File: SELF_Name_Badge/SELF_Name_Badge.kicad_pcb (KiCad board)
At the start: 2 copper layers, 105 x 70 mm, 1 part

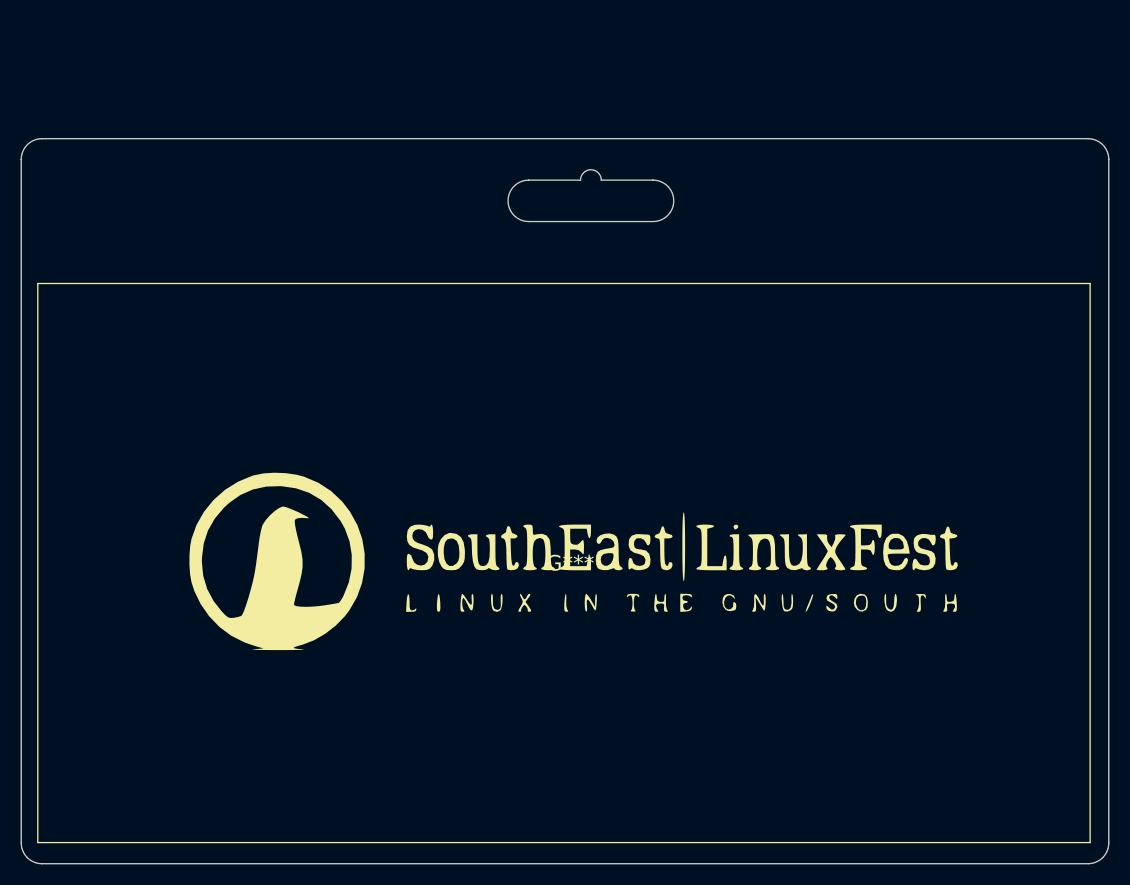
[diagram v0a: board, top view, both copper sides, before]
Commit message: cutout for adafruit QT esp32
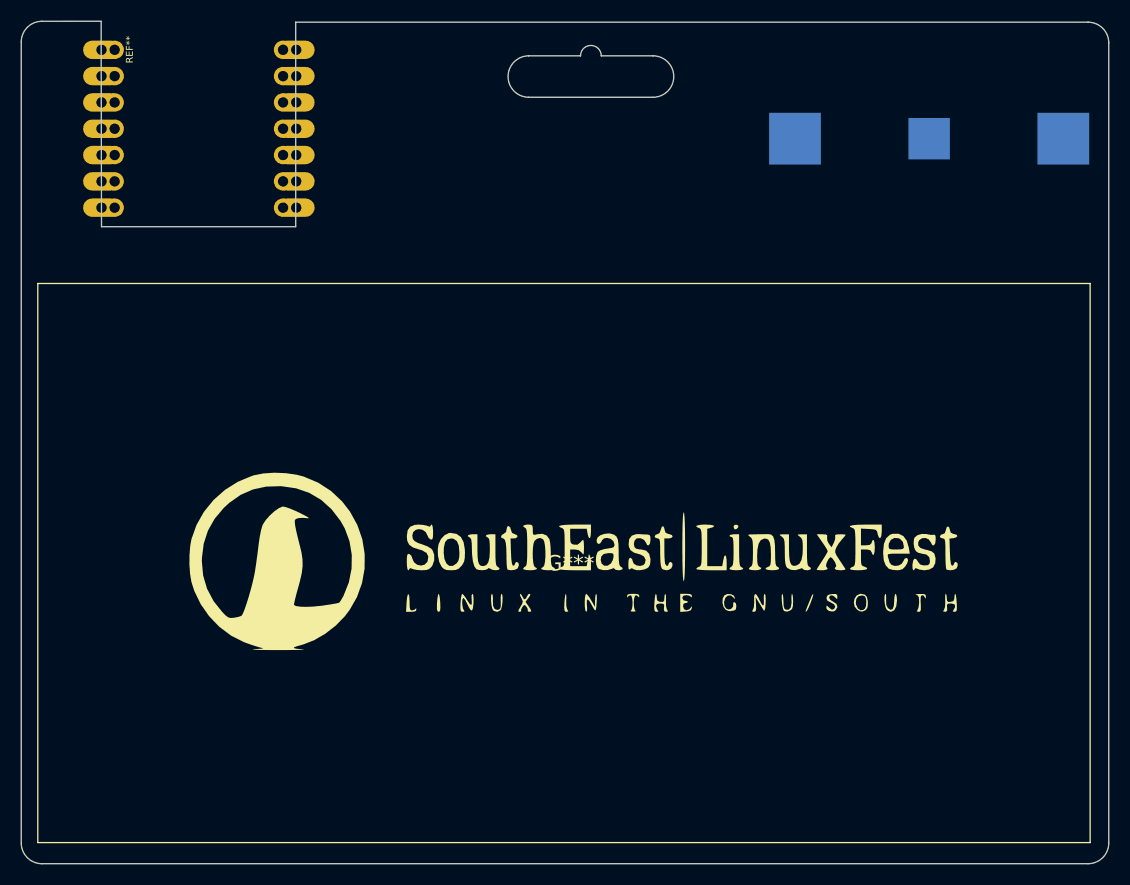
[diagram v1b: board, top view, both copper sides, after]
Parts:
- added REF**: 1X07_CASTEL, SELF_Name_Badge:1X07_CASTEL, F.Cu at (109.0, 39.0)
- added REF**: BatteryHolder_Multicomp_BC-2001_1x2032, Battery:BatteryHolder_Multicomp_BC-2001_1x2032, B.Cu at (187.7, 40.0)
- added REF**: 1X07_CASTEL, SELF_Name_Badge:1X07_CASTEL, B.Cu at (125.3, 39.0)
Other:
- board size 105 x 70 mm -> 105 x 81.3 mm
